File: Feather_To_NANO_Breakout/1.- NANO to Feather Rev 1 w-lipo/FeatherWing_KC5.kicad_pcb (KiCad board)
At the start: 2 copper layers, 49.5 x 22.9 mm, 17 parts, among them J1 feather long, J2 feather short, J3 Conn_01x15, J4 Conn_01x15, J5 Conn_01x02, U1 Feather_Cu, U10 Feather_Silks, U11 KiCadLogo, U2 Feather_Silks, U3 KiCadLogo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

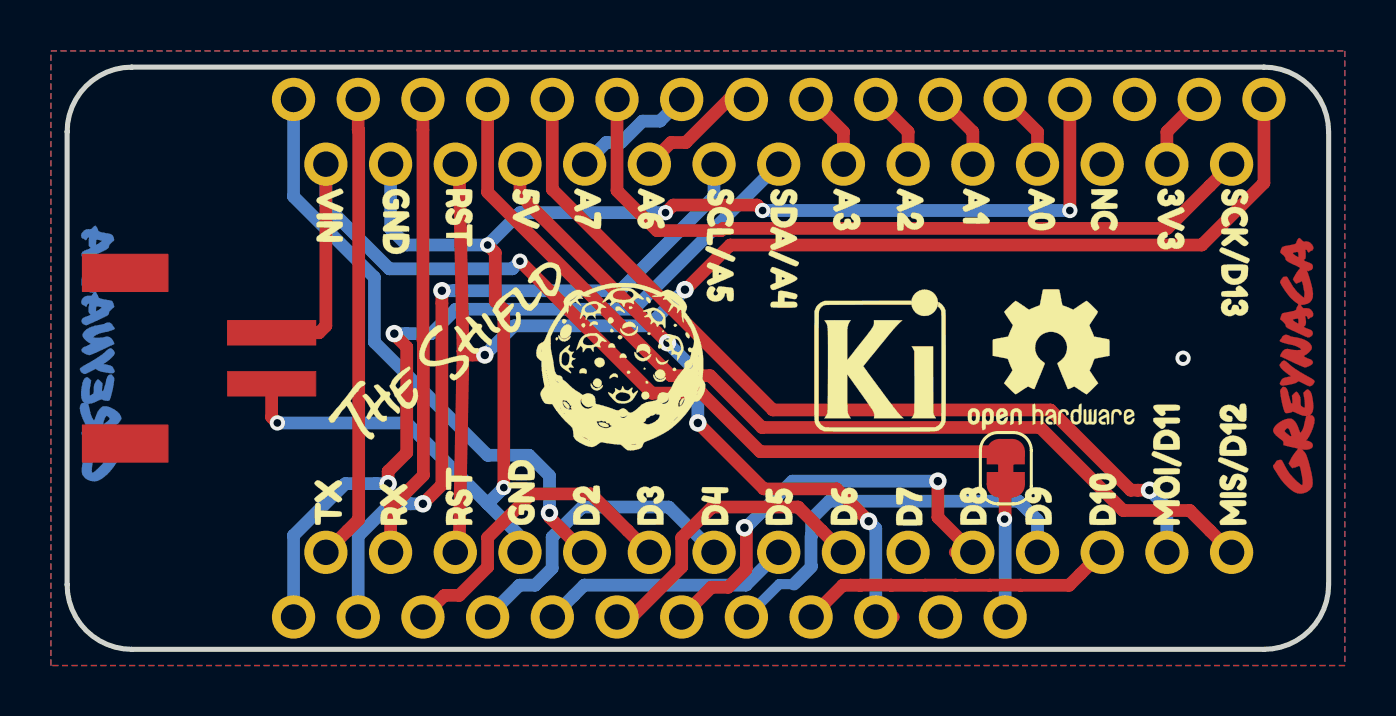
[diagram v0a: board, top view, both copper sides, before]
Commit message: Add Nano to Feather w-lipo
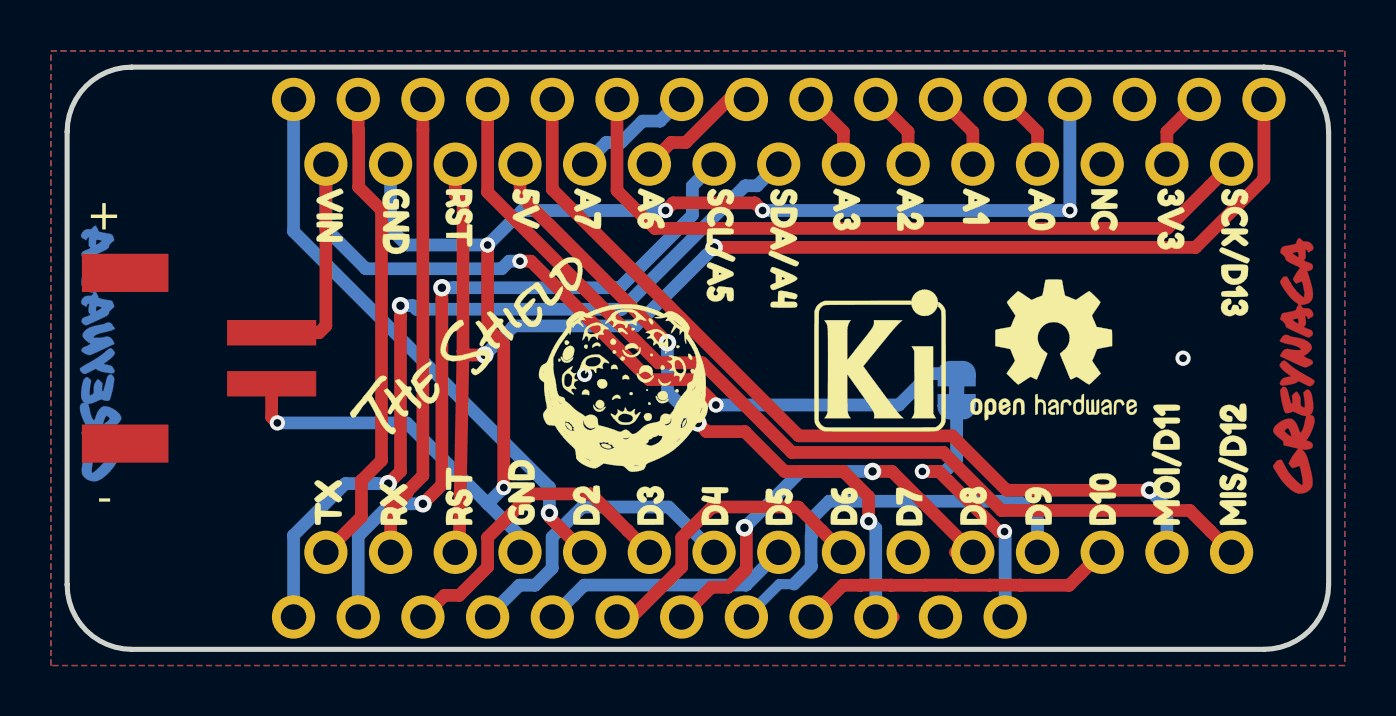
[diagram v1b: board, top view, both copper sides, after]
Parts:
- JP1: footprint Jumper:SolderJumper-2_P1.3mm_Bridged_RoundedPad1.0x1.5mm -> nano_feather_r_1:SolderJumper-2_P1.3mm_Bridged_RoundedPad1.0x1.5mm; moved to B.Cu
- moved JP1 3.62 mm to (148.6, 92.7)
- moved U5 0.86 mm to (130.6, 91.2)
- moved U4 0.84 mm to (136.0, 92.3)
- moved U8 0.81 mm to (134.6, 92.1)
- moved U9 0.66 mm to (142.9, 92.2)
- moved U6 0.39 mm to (152.4, 91.1)
- moved U11 0.15 mm to (127.0, 91.6)
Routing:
- net Net-(J2-Pad12): track 5.23 -> 11.2 mm, vias 1 -> 2
- net /VIN: track 41.0 -> 39.5 mm, vias 1 -> 2
- net /D2: track 23.5 -> 22.5 mm
- net /TX: track 18.3 -> 19.1 mm
- net +5V: track 26.0 -> 26.5 mm
- net /D8: track 17.4 -> 16.8 mm
- net GND: track 58.9 -> 59.0 mm, vias 7 -> 8
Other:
- board text added: "+"
- board text added: "-"
